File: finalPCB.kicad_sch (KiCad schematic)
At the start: 68 parts, among them J1 9V Battery, J2 FCR7350R, J3 FCR7350R, J4 FCR7350R, J5 Switch, K1 HFD4/005, K2 HFD4/005, K3 HFD4/005, Q1 IRLML6401, Q2 IRLML6401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

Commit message: Some routing done. There is still more schematic work to be done....
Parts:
- removed DZ1: PLV650A, symbol Device:D_Zener
- added C14: 10uf, Capacitor_SMD:C_0805_2012Metric_Pad1.18x1.45mm_HandSolder, symbol Device:C
- added D1: zener2.5, Diode_THT:D_A-405_P10.16mm_Horizontal, symbol Device:D_Zener
- C1, C13, C2, C3, C4, C5, C6: footprint (none) -> Capacitor_SMD:C_0805_2012Metric_Pad1.18x1.45mm_HandSolder
- D1: footprint (none) -> Diode_THT:D_A-405_P10.16mm_Horizontal
- J1, J5: footprint (none) -> Connector_PinSocket_2.54mm:PinSocket_1x02_P2.54mm_Vertical
- K1, K2, K3: footprint Homemade_foot:HFD4_005 -> HFD4_005:HFD4_005
- Q6: footprint (none) -> Package_TO_SOT_SMD:SOT-23-3
- R1, R2, R5, R6, R7, R8, R9: footprint (none) -> Resistor_SMD:R_0805_2012Metric_Pad1.20x1.40mm_HandSolder
- U1, U2: footprint (none) -> Package_SO:SOIC-8_3.9x4.9mm_P1.27mm
- U1: footprint (none) -> Package_DIP:DIP-14_W7.62mm_LongPads
- U5: footprint (none) -> Package_TO_SOT_SMD:TO-263-3_TabPin2
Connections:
- net +5V: now also K3.1 (+), R5.1, U5.3 (OUT), C14.1
- net CURRENT: now also C2.1, R1.2; no longer U1.6 (-), U1.7
- net GND: now also Q6.3 (S), C14.2, D1.2 (A)
- net HighRange: now also K3.4, U2.3 (+); no longer U2.2 (-)
- net LowRange: now also K3.2
- net RangeSel: now also Q6.2 (G)
- net VOLTAGE: now also K3.3
- net VOLTAGE IN: no longer R5.1
- net at R1.1, U1.1: now also D1.1 (K)
- net at Q6.1 (D): now also K3.8 (-)
- net at C6.1, R6.2, R7.1: now also U2.2 (-); no longer U2.3 (+)
- new net: U1.6 (-), U1.7
- now unconnected: U1.5 (+)
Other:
- moved on the sheet: K3, Q6, U1B

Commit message: V0.1 Done
The first full routing is complete. There is no LM35 sensor included.

PS.
The silkscreen art can be removed, but please no;)
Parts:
- added Q7, Q8: NMOS, Package_TO_SOT_SMD:SOT-23-3, symbol Simulation_SPICE:NMOS
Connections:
- net +5V: now also K1.1 (+), K2.1 (+)
- net D11: now also R9.1; no longer R7.1
- net D12: now also R10.1; no longer R6.1
- net D8: now also R6.1; no longer R10.1
- net D9: now also R7.1; no longer R9.1
- net GND: now also Q7.3 (S), Q8.3 (S); no longer K1.8 (-), K2.8 (-)
- net NEXT: now also SW2.1; no longer SW1.1
- net PREVIOUS: now also SW1.1; no longer SW2.1
- net Relay1: now reaches A1.25 (A6)
- net Relay1: now also Q7.2 (G)
- net Relay2: now reaches A1.26 (A7)
- net Relay2: now also Q8.2 (G)
- new net: K1.8 (-), Q8.1 (D)
- new net: K2.8 (-), Q7.1 (D)

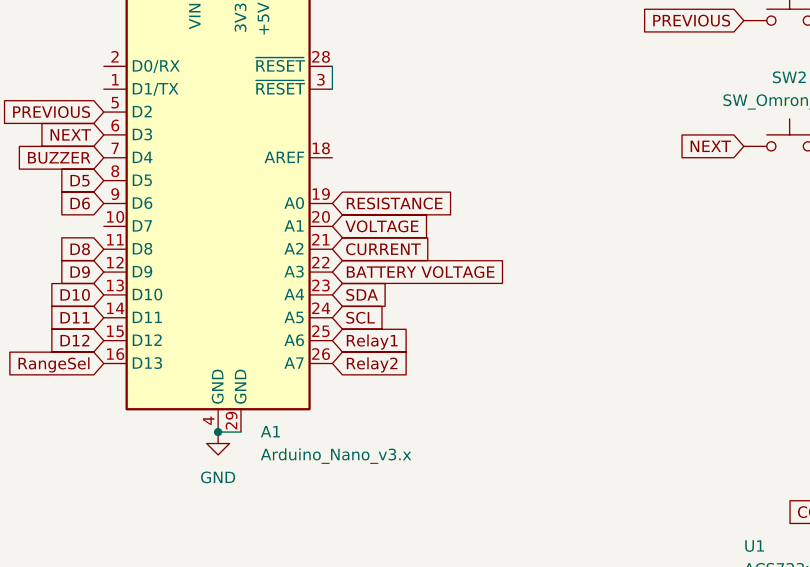
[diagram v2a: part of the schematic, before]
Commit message: Fixed minor issues
- Moved the relay further away from the current sensor.
- Added vias near the ground connection of the current sensort
- Swapped 3D models for the correct ones
- Moved ground plane away from the mounting holes
- Fixed pin capability related issue
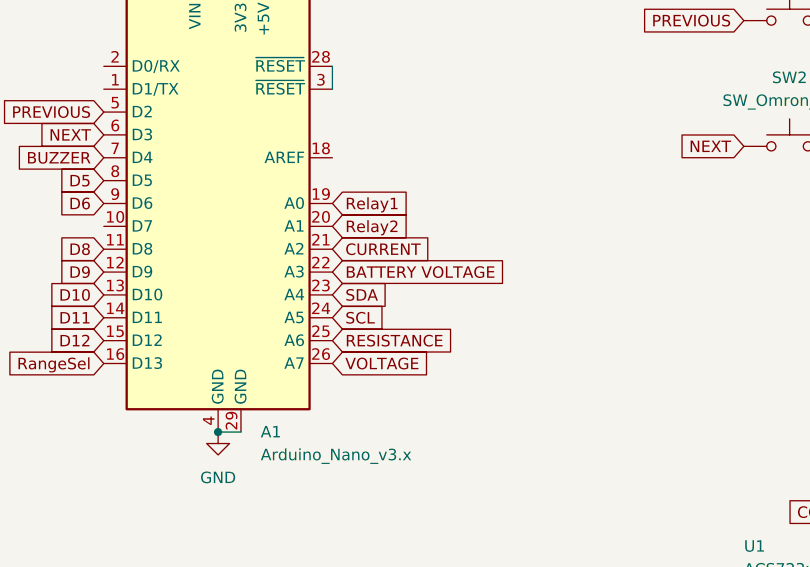
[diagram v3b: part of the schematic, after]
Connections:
- net RESISTANCE: now also A1.25 (A6); no longer A1.19 (A0)
- net Relay1: now also A1.19 (A0); no longer A1.25 (A6)
- net Relay2: now also A1.20 (A1); no longer A1.26 (A7)
- net VOLTAGE: now also A1.26 (A7); no longer A1.20 (A1)
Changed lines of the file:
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@@
     )
   )
-  (global_label "RESISTANCE" (shape input) (at 64.77 54.61 0) (fields_autoplaced)
+  (global_label "RESISTANCE" (shape input) (at 64.77 69.85 0) (fields_autoplaced)
     (effects (font (size 1.27 1.27)) (justify left))
-    (property "Intersheetrefs" "${INTERSHEET_REFS}" (at 79.0037 54.61 0)
+    (property "Intersheetrefs" "${INTERSHEET_REFS}" (at 79.0037 69.85 0)
       (effects (font (size 1.27 1.27)) (justify left) hide)
     )
   )
-  (global_label "VOLTAGE" (shape input) (at 64.77 57.15 0) (fields_autoplaced)
+  (global_label "VOLTAGE" (shape input) (at 64.77 72.39 0) (fields_autoplaced)
     (effects (font (size 1.27 1.27)) (justify left))
-    (property "Intersheetrefs" "${INTERSHEET_REFS}" (at 75.6776 57.15 0)
+    (property "Intersheetrefs" "${INTERSHEET_REFS}" (at 75.6776 72.39 0)
       (effects (font (size 1.27 1.27)) (justify left) hide)
     )
@@
     )
   )
-  (global_label "Relay2" (shape input) (at 64.77 72.39 0) (fields_autoplaced)
+  (global_label "Relay2" (shape input) (at 64.77 57.15 0) (fields_autoplaced)
     (effects (font (size 1.27 1.27)) (justify left))
-    (property "Intersheetrefs" "${INTERSHEET_REFS}" (at 74.1051 72.39 0)
+    (property "Intersheetrefs" "${INTERSHEET_REFS}" (at 74.1051 57.15 0)
       (effects (font (size 1.27 1.27)) (justify left) hide)
     )
@@
     )
   )
-  (global_label "Relay1" (shape input) (at 64.77 69.85 0) (fields_autoplaced)
+  (global_label "Relay1" (shape input) (at 64.77 54.61 0) (fields_autoplaced)
     (effects (font (size 1.27 1.27)) (justify left))
-    (property "Intersheetrefs" "${INTERSHEET_REFS}" (at 74.1051 69.85 0)
+    (property "Intersheetrefs" "${INTERSHEET_REFS}" (at 74.1051 54.61 0)
       (effects (font (size 1.27 1.27)) (justify left) hide)
     )

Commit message: V1.0 Complete
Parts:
- added C6: 10nF, Capacitor_SMD:C_0805_2012Metric_Pad1.18x1.45mm_HandSolder, symbol Device:C
- added C6: 0.1uF, Capacitor_SMD:C_0805_2012Metric_Pad1.18x1.45mm_HandSolder, symbol Device:C
- added J6: Conn_01x04_Pin, Connector_JST:JST_XH_B4B-XH-AM_1x04_P2.50mm_Vertical, symbol Connector:Conn_01x04_Pin
- added R2 (x2): 10k, Resistor_SMD:R_0805_2012Metric_Pad1.20x1.40mm_HandSolder, symbol Device:R
- added R2 (x2): 150, Resistor_SMD:R_0805_2012Metric_Pad1.20x1.40mm_HandSolder, symbol Device:R
- added U6: LM35-D, Package_SO:SOIC-8_3.9x4.9mm_P1.27mm, symbol Sensor_Temperature:LM35-D
- J1, J5: footprint Connector_PinSocket_2.54mm:PinSocket_1x02_P2.54mm_Vertical -> Connector_JST:JST_XH_B2B-XH-AM_1x02_P2.50mm_Vertical
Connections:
- net +5V: now also C6.1, J6.1 (Pin_1), U6.8 (+VS)
- net GND: now also C6.2, C6.2, J6.4 (Pin_4), R2.1, R2.1, U6.4 (GND)
- net Relay1: now also R2.2; no longer Q7.2 (G)
- net Relay2: now also A1.10 (D7), R2.2; no longer A1.20 (A1), Q8.2 (G)
- net SCL: now also J6.3 (Pin_3)
- net SDA: now also J6.2 (Pin_2)
- new net: Q8.2 (G), R2.1, R2.2
- new net: Q7.2 (G), R2.1, R2.2
- new net TEMPERATURE: A1.20 (A1), C6.1, U6.1 (Vout)
